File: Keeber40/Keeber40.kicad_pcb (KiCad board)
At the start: 2 copper layers, 257.1 x 92.9 mm, 86 parts, among them K1 KEYSW, K10 KEYSW, K11 KEYSW, K12 KEYSW, K13 KEYSW, K14 KEYSW, K15 KEYSW, K16 KEYSW, K17 KEYSW, K18 KEYSW, K19 KEYSW, K2 KEYSW, K20 KEYSW, K21 KEYSW, K22 KEYSW, K23 KEYSW, K24 KEYSW, K25 KEYSW, K26 KEYSW, K27 KEYSW, K28 KEYSW, K29 KEYSW, K3 KEYSW, K30 KEYSW, K31 KEYSW, K32 KEYSW, K33 KEYSW, K34 KEYSW, K35 KEYSW, K36 KEYSW, K37 KEYSW, K38 KEYSW, K39 KEYSW, K4 KEYSW, K5 KEYSW, K6 KEYSW, K7 KEYSW, K8 KEYSW, K9 KEYSW, M2 MountingHole_2.2mm_M2

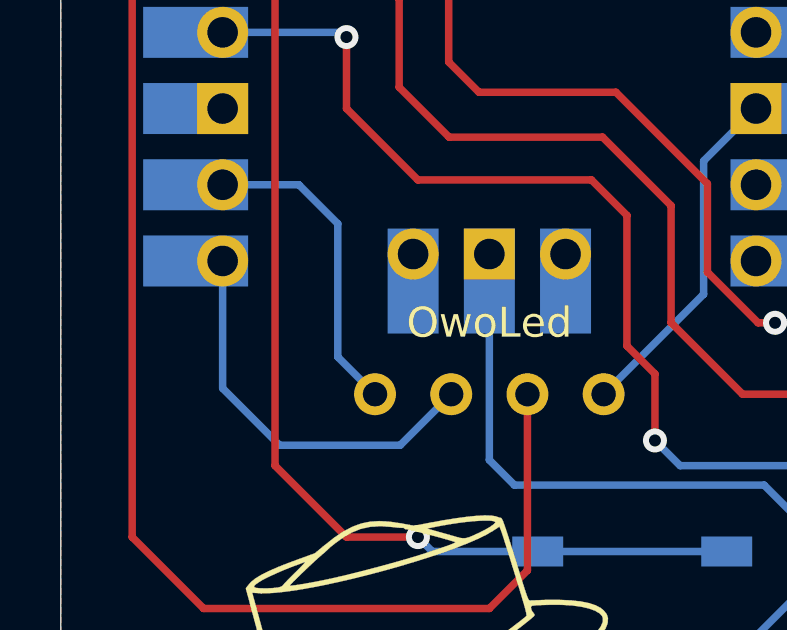
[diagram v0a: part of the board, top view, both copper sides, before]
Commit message: fixed pcb oled traces
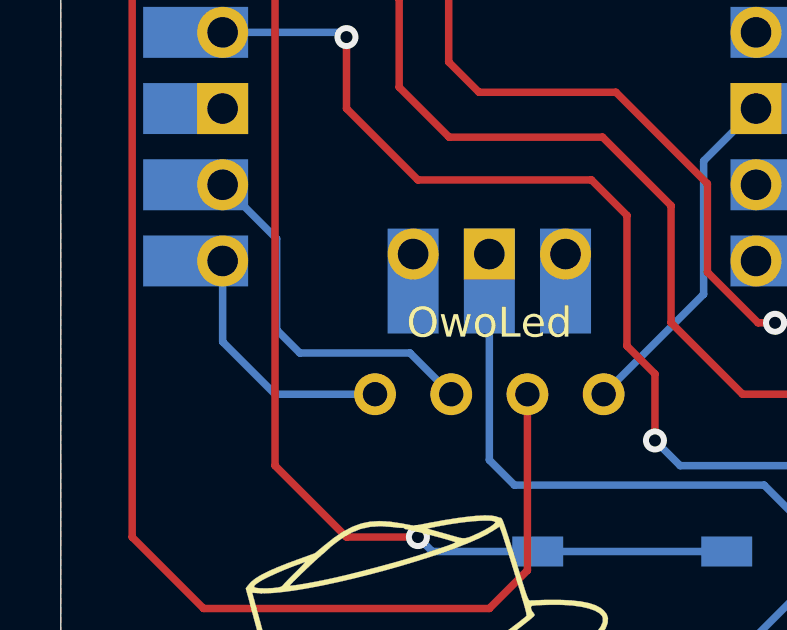
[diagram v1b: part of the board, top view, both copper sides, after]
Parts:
- renumbered Reset to SW1, PicOwo to U1
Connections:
- U1 pad 21: Net-(OL1-Pad2) -> Net-(OL1-Pad1)
- U1 pad 22: Net-(OL1-Pad1) -> Net-(OL1-Pad2)
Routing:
- net Net-(OL1-Pad1): track 10.6 -> 8.50 mm
- net Net-(OL1-Pad2): track 13.4 -> 12.3 mm
